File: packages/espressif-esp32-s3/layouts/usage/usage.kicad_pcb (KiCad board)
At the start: 2 copper layers, 9 parts

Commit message: clean up
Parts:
- removed R3: 10kΩ ±1% 100mW, UNI_ROYAL_0603WAF1002T5E:R0603

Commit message: missed build frozen
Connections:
- net IO15 renamed io[15]-line
- net IO16 renamed io[16]-line
- net IO17 renamed io[17]-line
- net IO18 renamed io[18]-line
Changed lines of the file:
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@@
     (net 4 "touch[4]-line")
     (net 5 "SCL")
-    (net 6 "IO16")
+    (net 6 "io[16]-line")
     (net 7 "IO40")
     (net 8 "IO45")
     (net 9 "MISO")
     (net 10 "touch[3]-line")
-    (net 11 "IO15")
+    (net 11 "io[15]-line")
     (net 12 "GND")
     (net 13 "touch[2]-line")
@@
     (net 34 "enable-output")
     (net 35 "touch[1]-line")
-    (net 36 "IO17")
-    (net 37 "IO18")
+    (net 36 "io[17]-line")
+    (net 37 "io[18]-line")
     (net 38 "IO47")
     (net 39 "VCC")
@@
             (size 1.5 0.9)
             (layers "F.Cu" "F.Paste" "F.Mask")
-            (net 11 "IO15")
+            (net 11 "io[15]-line")
         )
         (pad "9" smd rect
@@
             (size 1.5 0.9)
             (layers "F.Cu" "F.Paste" "F.Mask")
-            (net 6 "IO16")
+            (net 6 "io[16]-line")
         )
         (pad "10" smd rect
@@
             (size 1.5 0.9)
             (layers "F.Cu" "F.Paste" "F.Mask")
-            (net 36 "IO17")
+            (net 36 "io[17]-line")
         )
         (pad "11" smd rect
@@
             (size 1.5 0.9)
             (layers "F.Cu" "F.Paste" "F.Mask")
-            (net 37 "IO18")
+            (net 37 "io[18]-line")
         )
         (pad "12" smd rect
@@
     )
     (group "mcu"
-        (members "863ef09a-a21a-4266-9753-5586b7d89a47" "477e75b9-60b2-4ee8-b024-17684642524b" "25db5ef1-dac5-4d2f-9c25-e6824642524b" "d40f6dae-7721-4bb7-b3d6-6a3531f0ea98" "2cee3bab-a4ab-4e32-a1df-bf549da4dce4" "11ed3ef5-f69c-4401-84e5-5cb13cdcad96" "f0d15cca-73a6-454d-93cd-265e1890a9c0" "9dd64b77-681e-4c8e-86f8-706c113c38dd" "2a4d56b5-1693-4aed-80cf-27ac4642524b" "8a0d6e98-8f61-4f0c-9bdb-94af7fc975a8" "7d72b005-27a2-49dc-b552-7fa34642524b" "1bba4efd-587f-4765-961c-57c14642524b" "273f7587-2535-4704-8fae-2bf93404f37f" "03596390-84b4-45ff-80b5-d293e841043f" "8ea959a0-7b2b-4055-822e-e4c84642524b" "0aee14ae-1ea5-4bf5-849a-5b7dd7e0cc1b" "8eec20b1-8b68-4149-b6fc-a0ce65dda3fc" "062a0a4b-dc0f-4c8f-be45-ba78a5781b8e" "53d5d8bf-d236-4c6a-8da8-6f254642524b" "40743ee9-2b7c-4cfb-a849-d0664642524b" "49a331ff-ce82-41c6-8140-98650b2597e3" "9b35c64b-63d0-4b93-a177-b77ebbbaef8e" "02fb84f4-1e8b-43ae-ae0c-d6ca3b5a2606" "50750e7f-4310-4bae-b46d-bbac4aa93d06" "ddfb5585-be80-49e3-9be1-2394494a7db1" "85c10840-3feb-422f-a182-84994fa32321" "29e5af34-b020-40c0-b307-b0b74642524b" "e607f922-b750-4a64-97d4-3748037e4585" "71016be6-f9d3-447b-b164-4a3a2c5747ba" "e8c7cb12-06f5-4b61-bf6b-55403e4d6cf4" "34d0a2e0-799a-4ff2-ad28-0105de10991f" "8c437854-d33d-428e-9fc9-db713d8d85c6" "4179984b-3daf-4dd5-8733-e9b82d2f5d61" "c056658b-74d2-400d-aaa0-dcdcd9137af4" "6242d47b-05bf-4cd5-890f-b3660683824b" "2b8aa3a8-94e0-4efb-9bcd-aa6601d8e109" "0f02a8fb-0c21-4e8f-8fdb-757f579ce1c9")
+        (members "29e5af34-b020-40c0-b307-b0b74642524b" "11ed3ef5-f69c-4401-84e5-5cb13cdcad96" "53d5d8bf-d236-4c6a-8da8-6f254642524b" "8a0d6e98-8f61-4f0c-9bdb-94af7fc975a8" "ddfb5585-be80-49e3-9be1-2394494a7db1" "2cee3bab-a4ab-4e32-a1df-bf549da4dce4" "03596390-84b4-45ff-80b5-d293e841043f" "8eec20b1-8b68-4149-b6fc-a0ce65dda3fc" "9b35c64b-63d0-4b93-a177-b77ebbbaef8e" "02fb84f4-1e8b-43ae-ae0c-d6ca3b5a2606" "9dd64b77-681e-4c8e-86f8-706c113c38dd" "49a331ff-ce82-41c6-8140-98650b2597e3" "2a4d56b5-1693-4aed-80cf-27ac4642524b" "2b8aa3a8-94e0-4efb-9bcd-aa6601d8e109" "85c10840-3feb-422f-a182-84994fa32321" "71016be6-f9d3-447b-b164-4a3a2c5747ba" "f0d15cca-73a6-454d-93cd-265e1890a9c0" "d40f6dae-7721-4bb7-b3d6-6a3531f0ea98" "e8c7cb12-06f5-4b61-bf6b-55403e4d6cf4" "50750e7f-4310-4bae-b46d-bbac4aa93d06" "0f02a8fb-0c21-4e8f-8fdb-757f579ce1c9" "8ea959a0-7b2b-4055-822e-e4c84642524b" "6242d47b-05bf-4cd5-890f-b3660683824b" "7d72b005-27a2-49dc-b552-7fa34642524b" "477e75b9-60b2-4ee8-b024-17684642524b" "273f7587-2535-4704-8fae-2bf93404f37f" "40743ee9-2b7c-4cfb-a849-d0664642524b" "1bba4efd-587f-4765-961c-57c14642524b" "4179984b-3daf-4dd5-8733-e9b82d2f5d61" "c056658b-74d2-400d-aaa0-dcdcd9137af4" "0aee14ae-1ea5-4bf5-849a-5b7dd7e0cc1b" "e607f922-b750-4a64-97d4-3748037e4585" "25db5ef1-dac5-4d2f-9c25-e6824642524b" "863ef09a-a21a-4266-9753-5586b7d89a47" "062a0a4b-dc0f-4c8f-be45-ba78a5781b8e" "8c437854-d33d-428e-9fc9-db713d8d85c6" "34d0a2e0-799a-4ff2-ad28-0105de10991f")
     )
 )

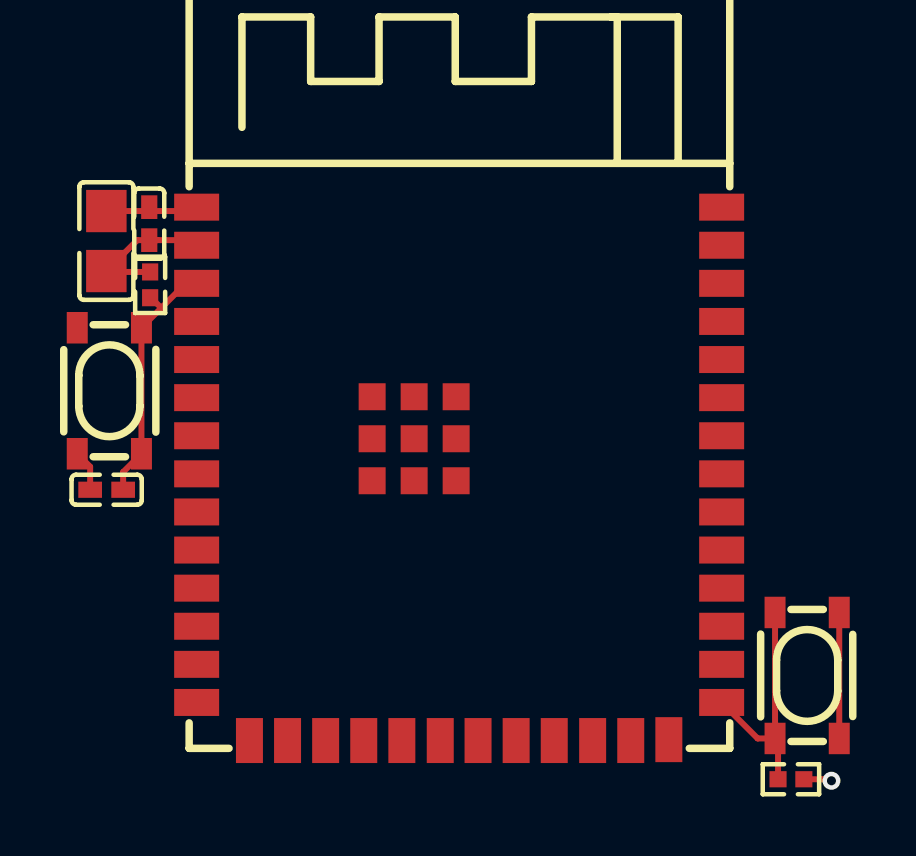
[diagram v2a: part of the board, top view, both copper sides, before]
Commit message: espressif-esp32-s3: package update to v0.2.0, ato:^0.14.0 (#320)
Build targets:
  default = rc0
  usage = rc0
Package Verify: rc0
Version: 0.1.0 -> 0.2.0
Requires ato: ^0.14.0
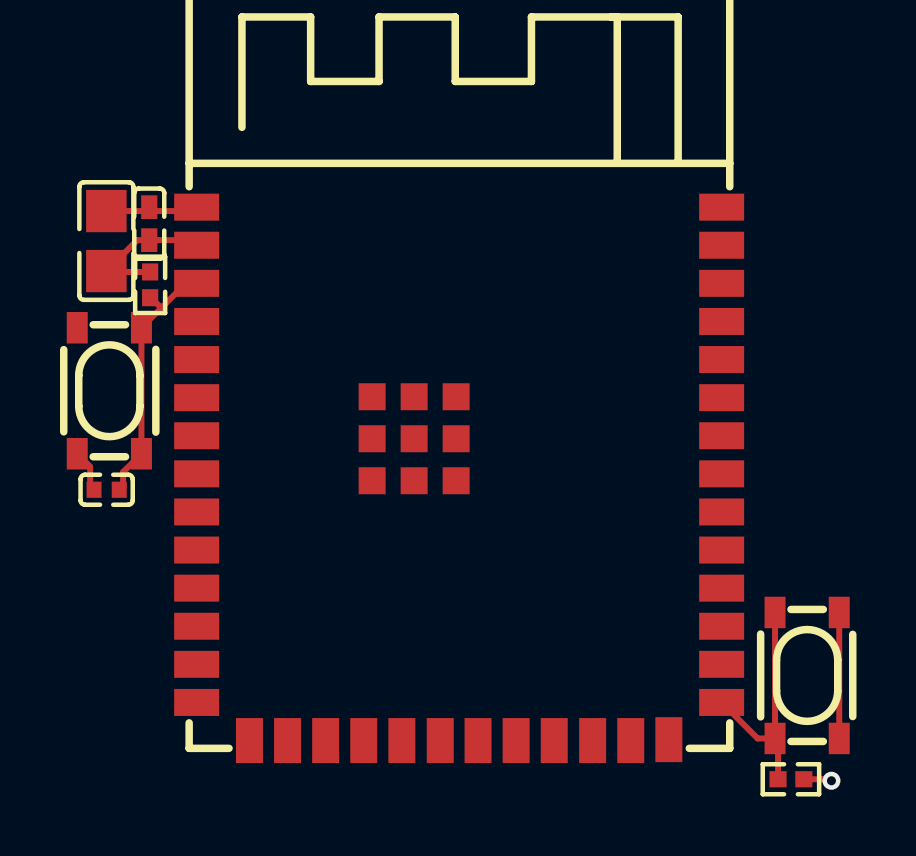
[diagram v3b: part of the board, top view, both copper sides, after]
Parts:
- C1: value 10µF ±10% 25V X5R -> {8.999..1.1}F
- C2: value 100nF ±10% 16V X7R -> 1±10.0%F
- C3: value 1µF ±10% 25V X5R -> {8.999..1.1}F
- R1, R2: value 10kΩ ±1% 62.5mW -> 10000±1.0%Ω
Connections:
- net GND renamed lv
- net IO21 renamed 23
- net IO35 renamed 28
- net IO36 renamed 29
- net IO37 renamed 30
- net IO38 renamed 31
- net IO39 renamed 32
- net IO40 renamed 33
- net IO41 renamed 34
- net IO42 renamed 35
- net IO45 renamed 26
- net IO46 renamed 16
- net IO47 renamed 24
- net IO48 renamed 25
- net USB_D_N renamed DATA_N
- net USB_D_P renamed DATA_P
- net VCC renamed hv
- net enable-output renamed c_en-power-hv
- net io[0]-output renamed output
- net touch[10]-line renamed line

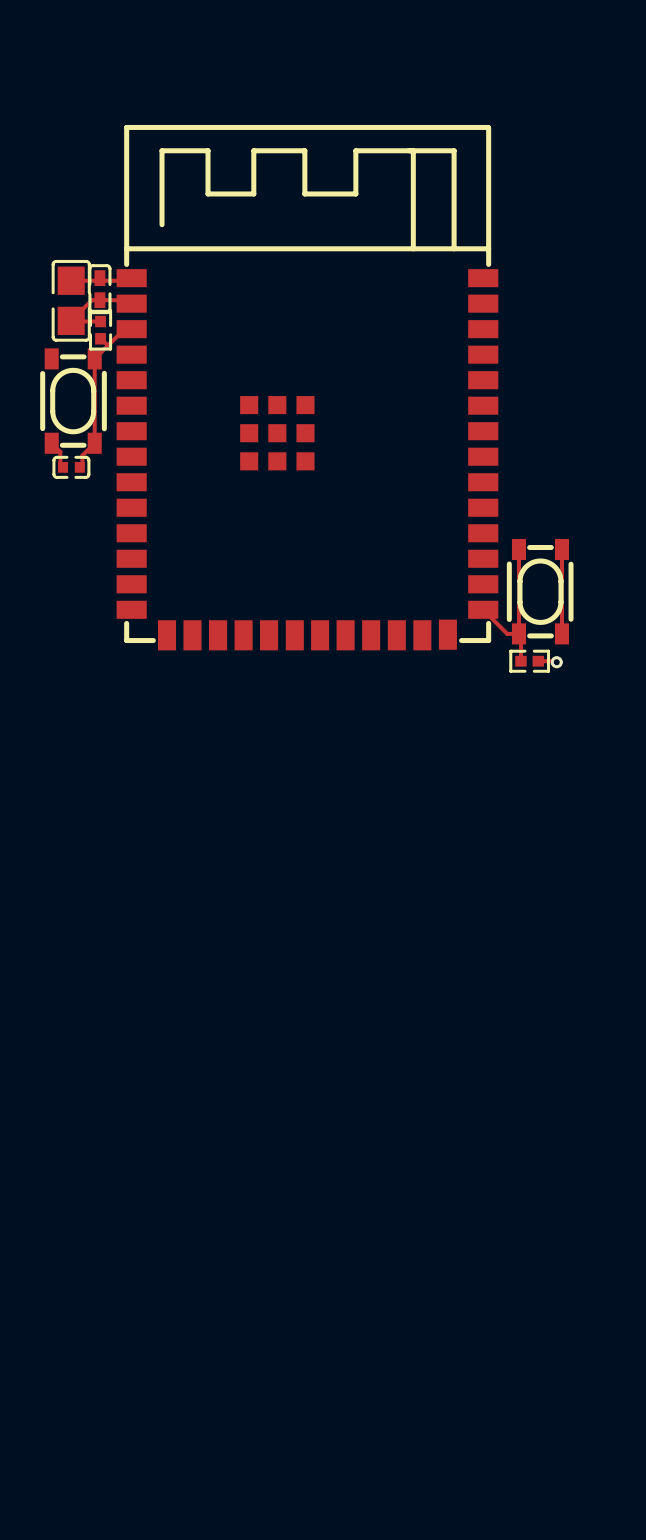
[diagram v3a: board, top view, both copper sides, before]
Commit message: fix buttons and esp32s3 packages
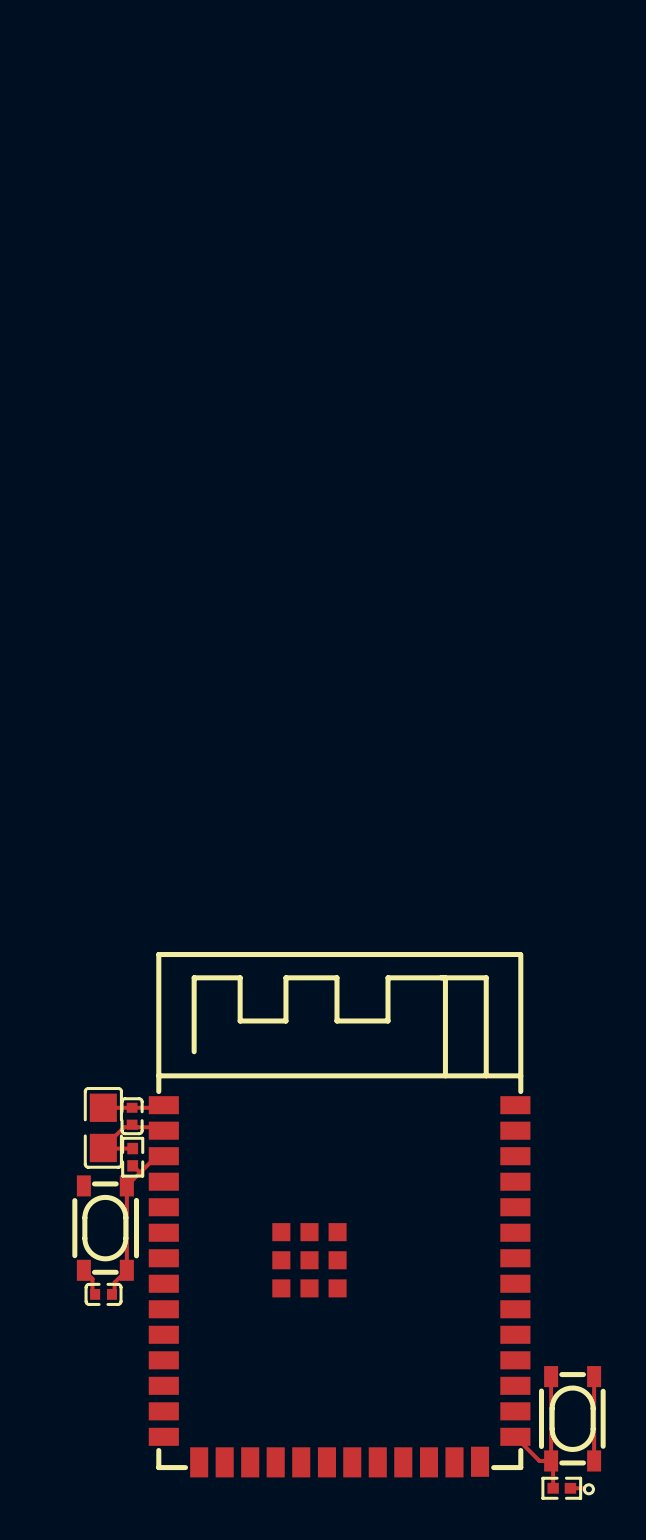
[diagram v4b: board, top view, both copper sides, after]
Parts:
- C1: value {8.999..1.1}F -> 9.999F
- C2: value 1±10.0%F -> 1F
- C3: value {8.999..1.1}F -> 1e-06F
- R1, R2: value 10000±1.0%Ω -> 10000Ω
- moved C1 41.2 mm to (-10.2, -6.59)
- moved C2 41.2 mm to (-8.73, -7.17)
- moved C3 41.2 mm to (-10.2, 1.70)
- moved R1 41.2 mm to (12.7, 11.3)
- moved SW1 41.2 mm to (13.2, 7.89)
- moved SW2 41.2 mm to (-10.1, -1.60)
- moved U1 41.2 mm to (1.60, 1.17)
- moved R2 41.2 mm to (-8.70, -5.13)
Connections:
- C2 pad 1: hv -> (no net)
- C2 pad 2: lv -> (no net)

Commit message: fix frozen and lint
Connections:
- C2 pad 1: (no net) -> hv
- C2 pad 2: (no net) -> lv
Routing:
- net hv: track 6.19 -> 0.00 mm, vias 1 -> 0
- net 37: track 0.00 -> 6.19 mm, vias 0 -> 1
